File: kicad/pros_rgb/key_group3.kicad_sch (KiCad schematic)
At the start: 6 parts

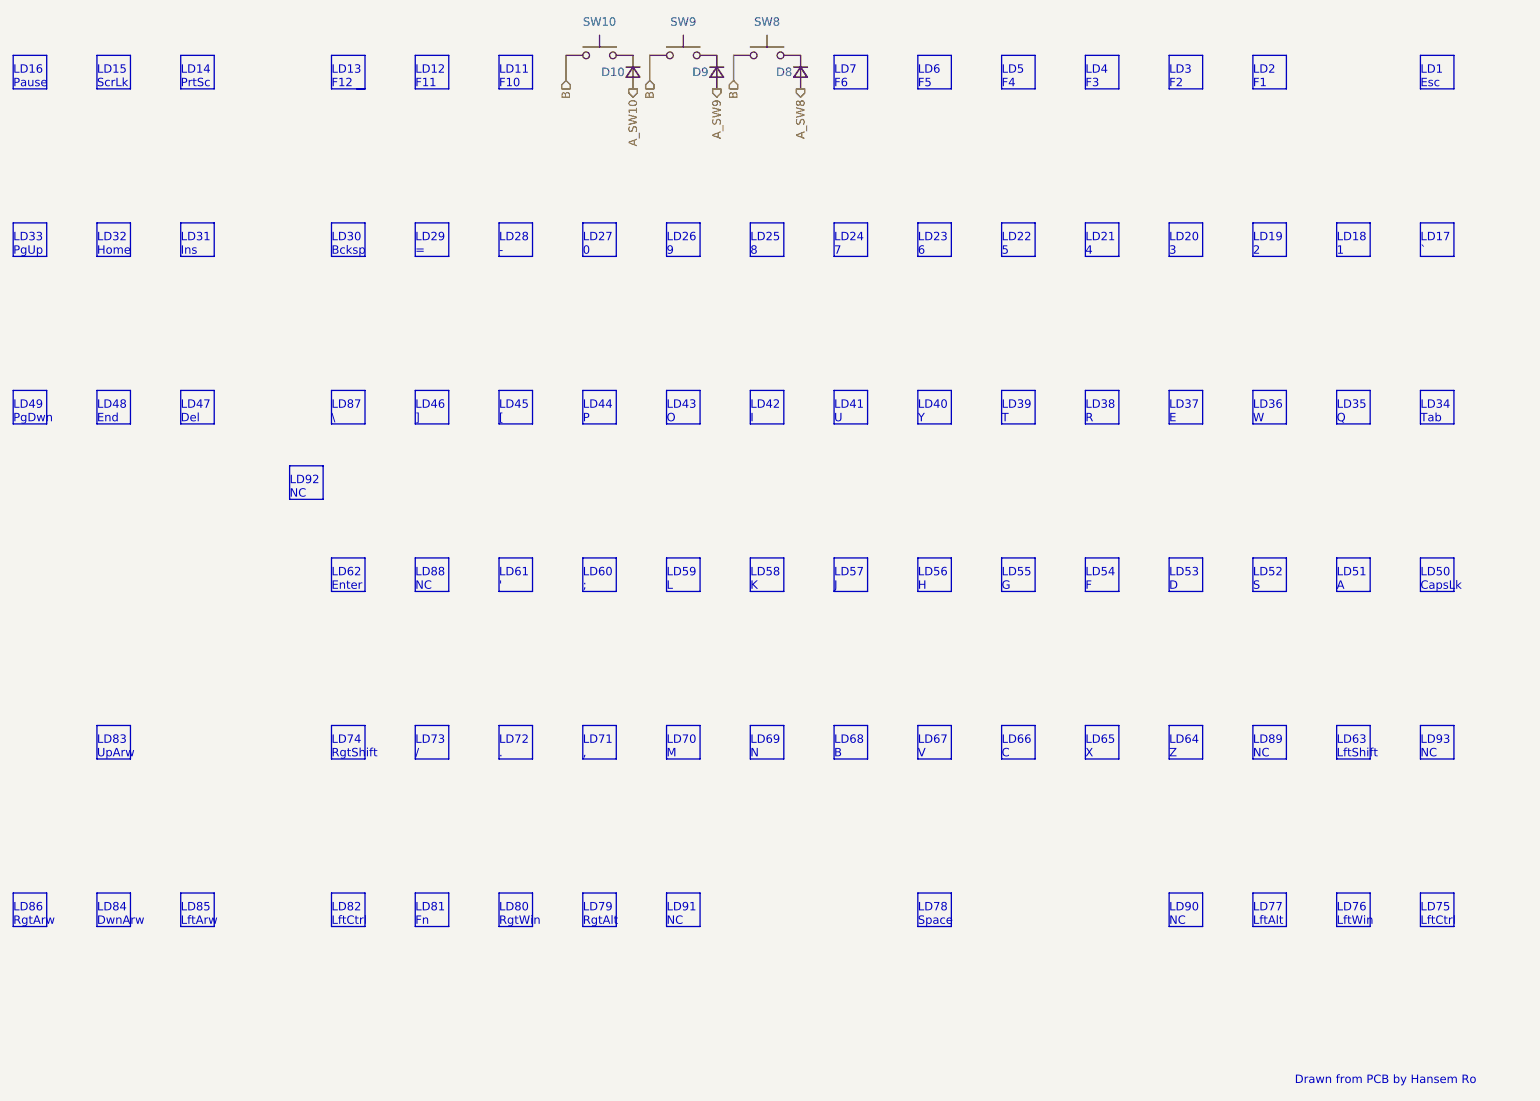
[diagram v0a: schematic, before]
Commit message: kicad/pros_rgb: update key groupings
These new groupings are based off ordering in firmware:
https://github.com/hansemro/pok3r_re_firmware/blob/4b68aa4baf7d28dc8dbf8eebcb1fdb59e7bcd629/disassemble/cmprosrgb/v122/cmprosrgb_v122.txt#L14599-L14629
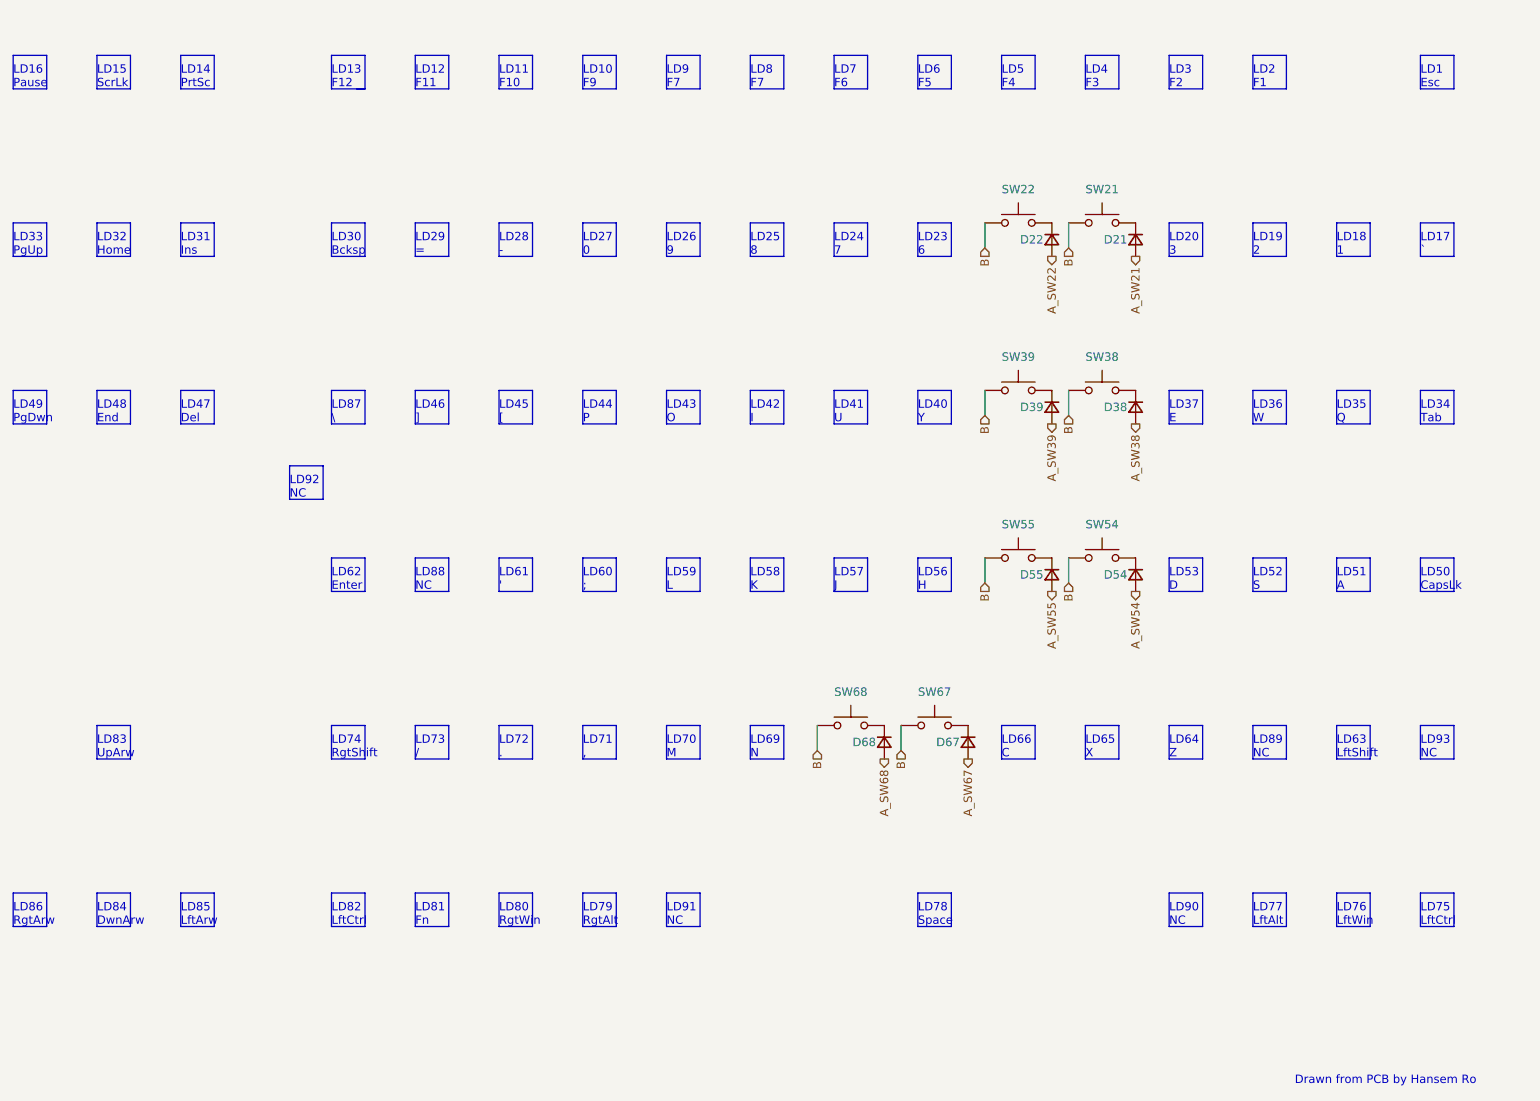
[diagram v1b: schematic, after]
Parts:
- removed D10, D8, D9: ~, symbol Device:D_Small
- removed SW10, SW8, SW9: ~, symbol Switch:SW_Push
- added D21, D22, D38, D39, D54, D55, D67, D68: (no value), symbol Device:D_Small
- added SW21, SW22, SW38, SW39, SW54, SW55, SW67, SW68: (no value), symbol Switch:SW_Push
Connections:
- net B: now also SW21.1, SW22.1, SW38.1, SW39.1, SW54.1, SW55.1, SW67.1, SW68.1
- new net: D68.1 (K), SW68.2
- new net: D39.1 (K), SW39.2
- new net: D38.1 (K), SW38.2
- new net: D55.1 (K), SW55.2
- new net: D22.1 (K), SW22.2
- new net: D54.1 (K), SW54.2
- new net: D21.1 (K), SW21.2
- new net: D67.1 (K), SW67.2
- new net A_SW21: D21.2 (A)
- new net A_SW22: D22.2 (A)
- new net A_SW38: D38.2 (A)
- new net A_SW39: D39.2 (A)
- new net A_SW54: D54.2 (A)
- new net A_SW55: D55.2 (A)
- new net A_SW67: D67.2 (A)
- new net A_SW68: D68.2 (A)
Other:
- note added: "LD10 F9"
- note added: "LD8 F7"
- note added: "LD9 F7"
- note removed: "LD21 4"
- note removed: "LD22 5"
- note removed: "LD38 R"
- note removed: "LD39 T"
- note removed: "LD54 F"
- note removed: "LD55 G"
- note removed: "LD67 V"
- note removed: "LD68 B"

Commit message: kicad/pros_rgb: mark as Rev. B
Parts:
- D21, D22, D38, D39, D54, D55, D67, D68, SW21, SW22, SW38, SW39, SW54, SW55, SW67, SW68: value (none) -> ~
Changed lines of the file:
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@@
     (in_bom yes) (on_board yes)
     (property "Reference" "SW68" (id 0) (at 185.42 120.65 0))
-    (property "Value" "" (id 1) (at 185.42 120.65 0))
+    (property "Value" "~" (id 1) (at 185.42 120.65 0))
     (property "Footprint" "" (id 2) (at 185.42 120.65 0)
       (effects (font (size 1.27 1.27)) hide)
@@
       (effects (font (size 1.27 1.27)) (justify right))
     )
-    (property "Value" "" (id 1) (at 218.44 78.7399 90)
+    (property "Value" "~" (id 1) (at 218.44 78.7399 90)
       (effects (font (size 1.27 1.27)) (justify left))
     )
@@
       (effects (font (size 1.27 1.27)) (justify right))
     )
-    (property "Value" "" (id 1) (at 231.14 78.7399 90)
+    (property "Value" "~" (id 1) (at 231.14 78.7399 90)
       (effects (font (size 1.27 1.27)) (justify left))
     )
@@
       (effects (font (size 1.27 1.27)) (justify right))
     )
-    (property "Value" "" (id 1) (at 193.04 129.5399 90)
+    (property "Value" "~" (id 1) (at 193.04 129.5399 90)
       (effects (font (size 1.27 1.27)) (justify left))
     )
@@
       (effects (font (size 1.27 1.27)) (justify right))
     )
-    (property "Value" "" (id 1) (at 218.44 104.1399 90)
+    (property "Value" "~" (id 1) (at 218.44 104.1399 90)
       (effects (font (size 1.27 1.27)) (justify left))
     )
@@
     (in_bom yes) (on_board yes)
     (property "Reference" "SW22" (id 0) (at 210.82 44.45 0))
-    (property "Value" "" (id 1) (at 210.82 44.45 0))
+    (property "Value" "~" (id 1) (at 210.82 44.45 0))
     (property "Footprint" "" (id 2) (at 210.82 44.45 0)
       (effects (font (size 1.27 1.27)) hide)
@@
       (effects (font (size 1.27 1.27)) (justify right))
     )
-    (property "Value" "" (id 1) (at 231.14 104.1399 90)
+    (property "Value" "~" (id 1) (at 231.14 104.1399 90)
       (effects (font (size 1.27 1.27)) (justify left))
     )
@@
     (in_bom yes) (on_board yes)
     (property "Reference" "SW38" (id 0) (at 223.52 69.85 0))
-    (property "Value" "" (id 1) (at 223.52 69.85 0))
+    (property "Value" "~" (id 1) (at 223.52 69.85 0))
     (property "Footprint" "" (id 2) (at 223.52 69.85 0)
       (effects (font (size 1.27 1.27)) hide)
@@
     (in_bom yes) (on_board yes)
     (property "Reference" "SW54" (id 0) (at 223.52 95.25 0))
-    (property "Value" "" (id 1) (at 223.52 95.25 0))
+    (property "Value" "~" (id 1) (at 223.52 95.25 0))
     (property "Footprint" "" (id 2) (at 223.52 95.25 0)
       (effects (font (size 1.27 1.27)) hide)
@@
       (effects (font (size 1.27 1.27)) (justify right))
     )
-    (property "Value" "" (id 1) (at 231.14 53.3399 90)
+    (property "Value" "~" (id 1) (at 231.14 53.3399 90)
       (effects (font (size 1.27 1.27)) (justify left))
     )
@@
     (in_bom yes) (on_board yes)
     (property "Reference" "SW55" (id 0) (at 210.82 95.25 0))
-    (property "Value" "" (id 1) (at 210.82 95.25 0))
+    (property "Value" "~" (id 1) (at 210.82 95.25 0))
     (property "Footprint" "" (id 2) (at 210.82 95.25 0)
       (effects (font (size 1.27 1.27)) hide)
@@
       (effects (font (size 1.27 1.27)) (justify right))
     )
-    (property "Value" "" (id 1) (at 205.74 129.5399 90)
+    (property "Value" "~" (id 1) (at 205.74 129.5399 90)
       (effects (font (size 1.27 1.27)) (justify left))
     )
@@
     (in_bom yes) (on_board yes)
     (property "Reference" "SW21" (id 0) (at 223.52 44.45 0))
-    (property "Value" "" (id 1) (at 223.52 44.45 0))
+    (property "Value" "~" (id 1) (at 223.52 44.45 0))
     (property "Footprint" "" (id 2) (at 223.52 44.45 0)
       (effects (font (size 1.27 1.27)) hide)
@@
     (in_bom yes) (on_board yes)
     (property "Reference" "SW67" (id 0) (at 198.12 120.65 0))
-    (property "Value" "" (id 1) (at 198.12 120.65 0))
+    (property "Value" "~" (id 1) (at 198.12 120.65 0))
     (property "Footprint" "" (id 2) (at 198.12 120.65 0)
       (effects (font (size 1.27 1.27)) hide)
@@
     (in_bom yes) (on_board yes)
     (property "Reference" "SW39" (id 0) (at 210.82 69.85 0))
-    (property "Value" "" (id 1) (at 210.82 69.85 0))
+    (property "Value" "~" (id 1) (at 210.82 69.85 0))
     (property "Footprint" "" (id 2) (at 210.82 69.85 0)
       (effects (font (size 1.27 1.27)) hide)
@@
       (effects (font (size 1.27 1.27)) (justify right))
     )
-    (property "Value" "" (id 1) (at 218.44 53.3399 90)
-      (effects (font (size 1.27 1.27)) (justify left))
-    )
+    (property "Value" "~" (id 1) (at 218.44 53.3399 90)
+      (effects (font (size 1.27 1.27)) (justify left))
+    )

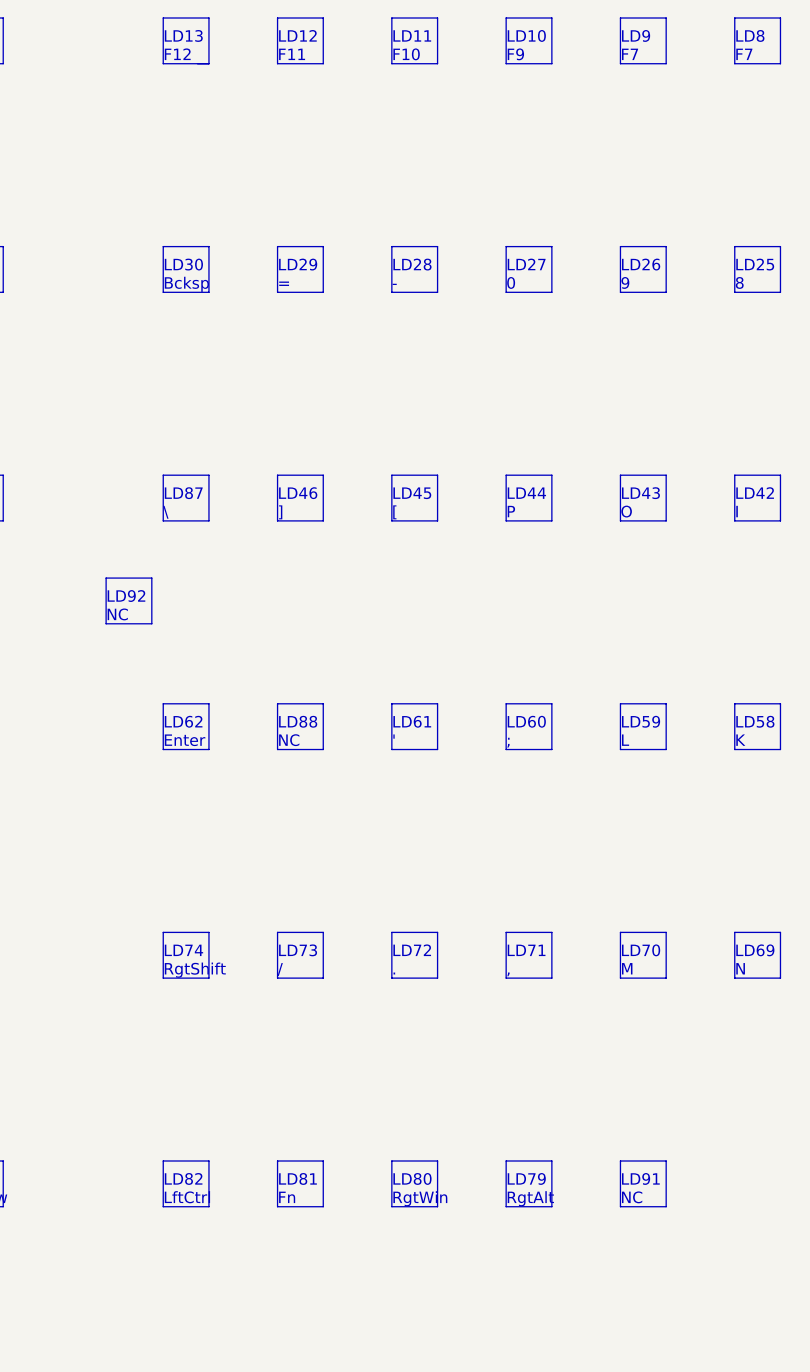
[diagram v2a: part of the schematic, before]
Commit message: kicad/pros_rgb: fix typos
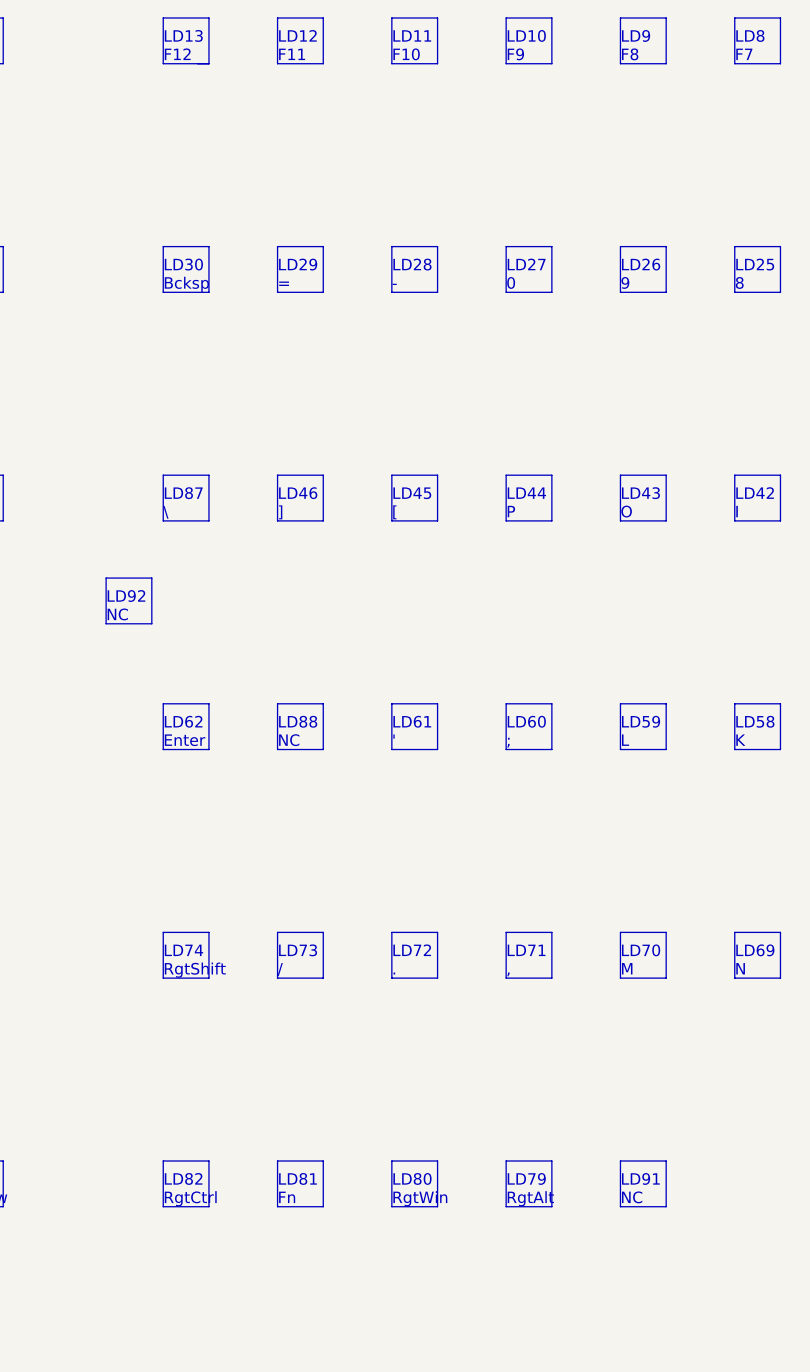
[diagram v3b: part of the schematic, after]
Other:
- note added: "LD82 RgtCtrl"
- note added: "LD9 F8"
- note removed: "LD82 LftCtrl"
- note removed: "LD9 F7"
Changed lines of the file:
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@@
     (effects (font (size 1.27 1.27)) (justify left bottom))
   )
-  (text "LD9\nF7" (at 157.48 29.21 0)
+  (text "LD9\nF8" (at 157.48 29.21 0)
     (effects (font (size 1.27 1.27)) (justify left bottom))
   )
@@
     (effects (font (size 1.27 1.27)) (justify left bottom))
   )
-  (text "LD82\nLftCtrl" (at 106.68 156.21 0)
+  (text "LD82\nRgtCtrl" (at 106.68 156.21 0)
     (effects (font (size 1.27 1.27)) (justify left bottom))
   )
